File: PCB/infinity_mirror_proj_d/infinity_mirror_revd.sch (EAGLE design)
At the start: 28 parts, among them J1 5.5x2.1mm Barrel, Q1 800mA/40V, Q2 800mA/40V, U1 3.3LDO

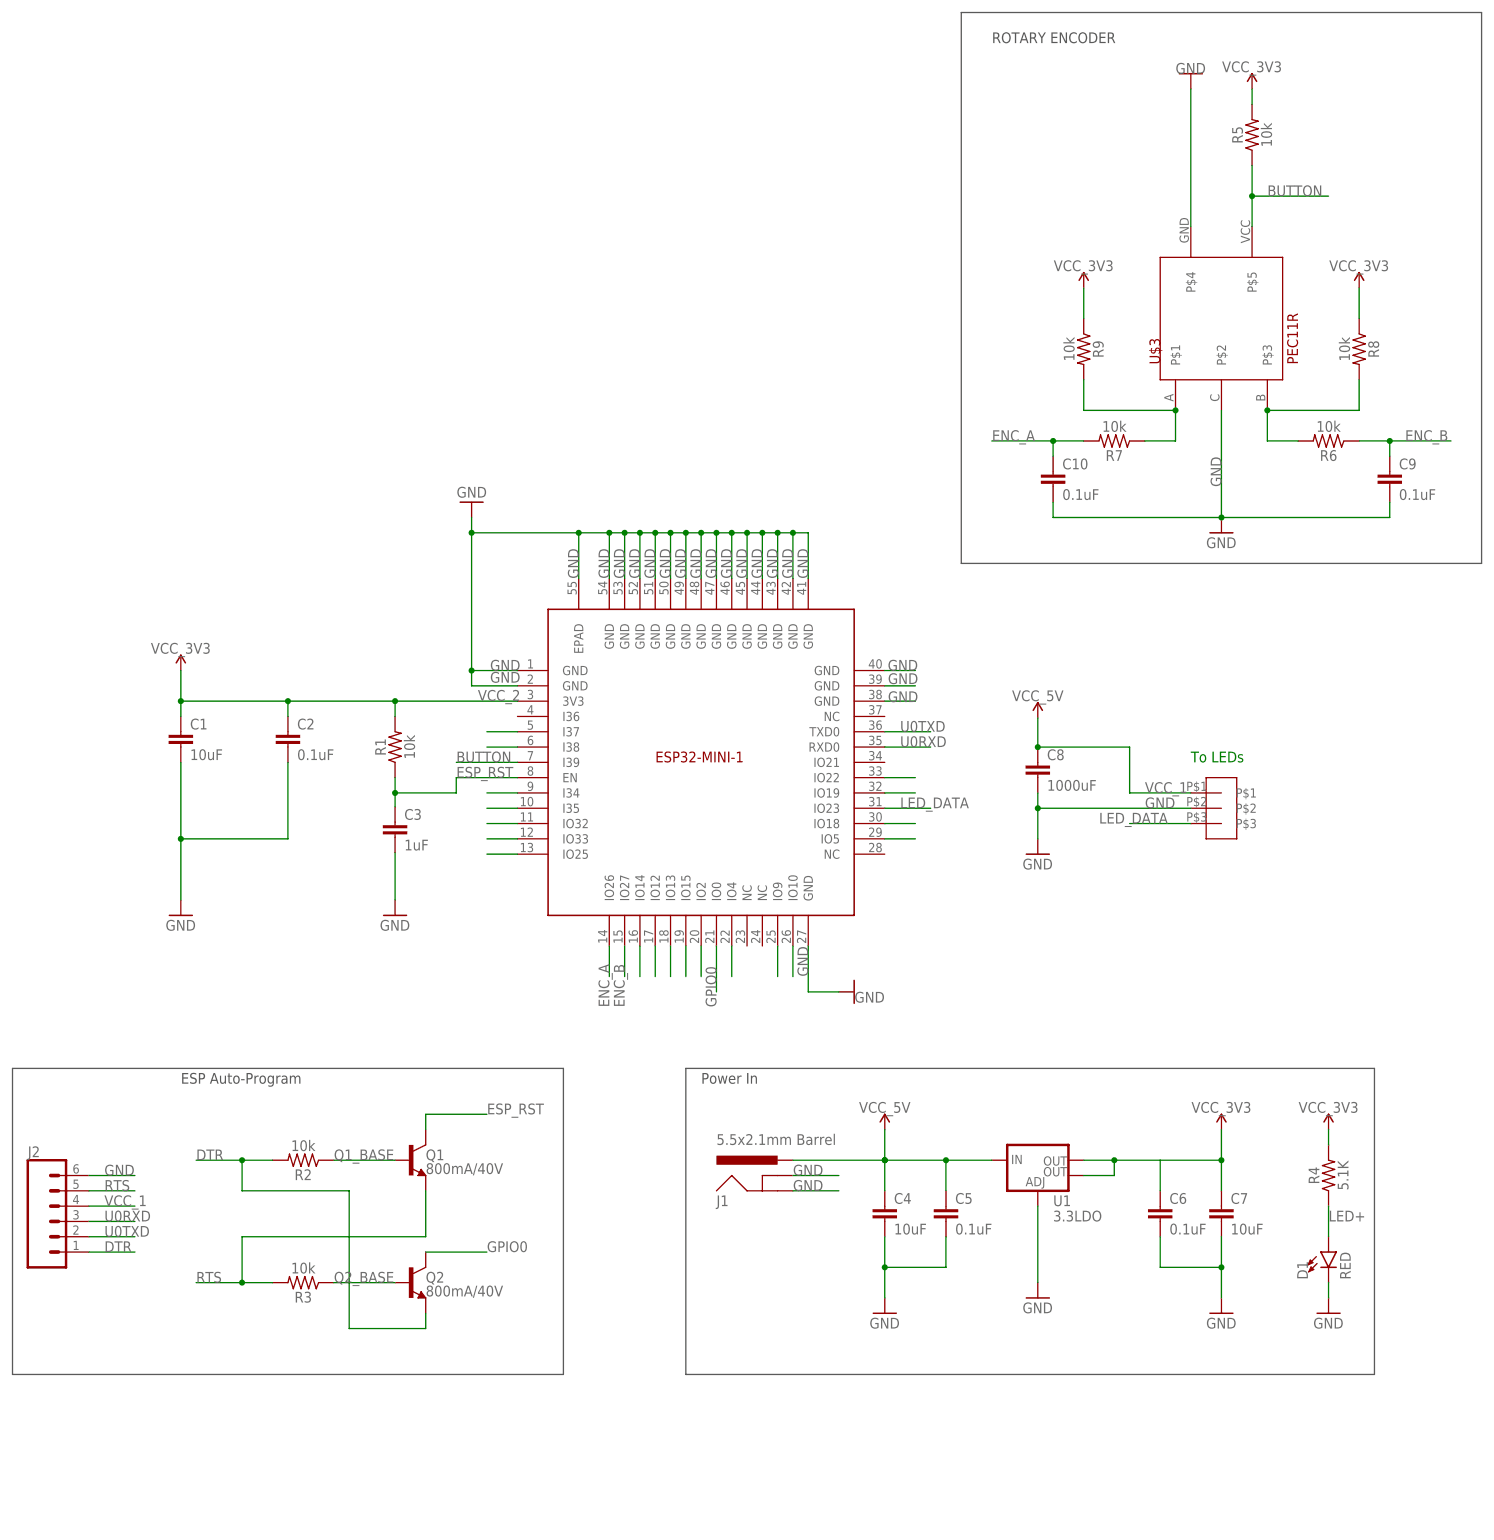
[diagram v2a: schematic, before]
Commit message: added logic level shifting for LEDs and buttons for programming
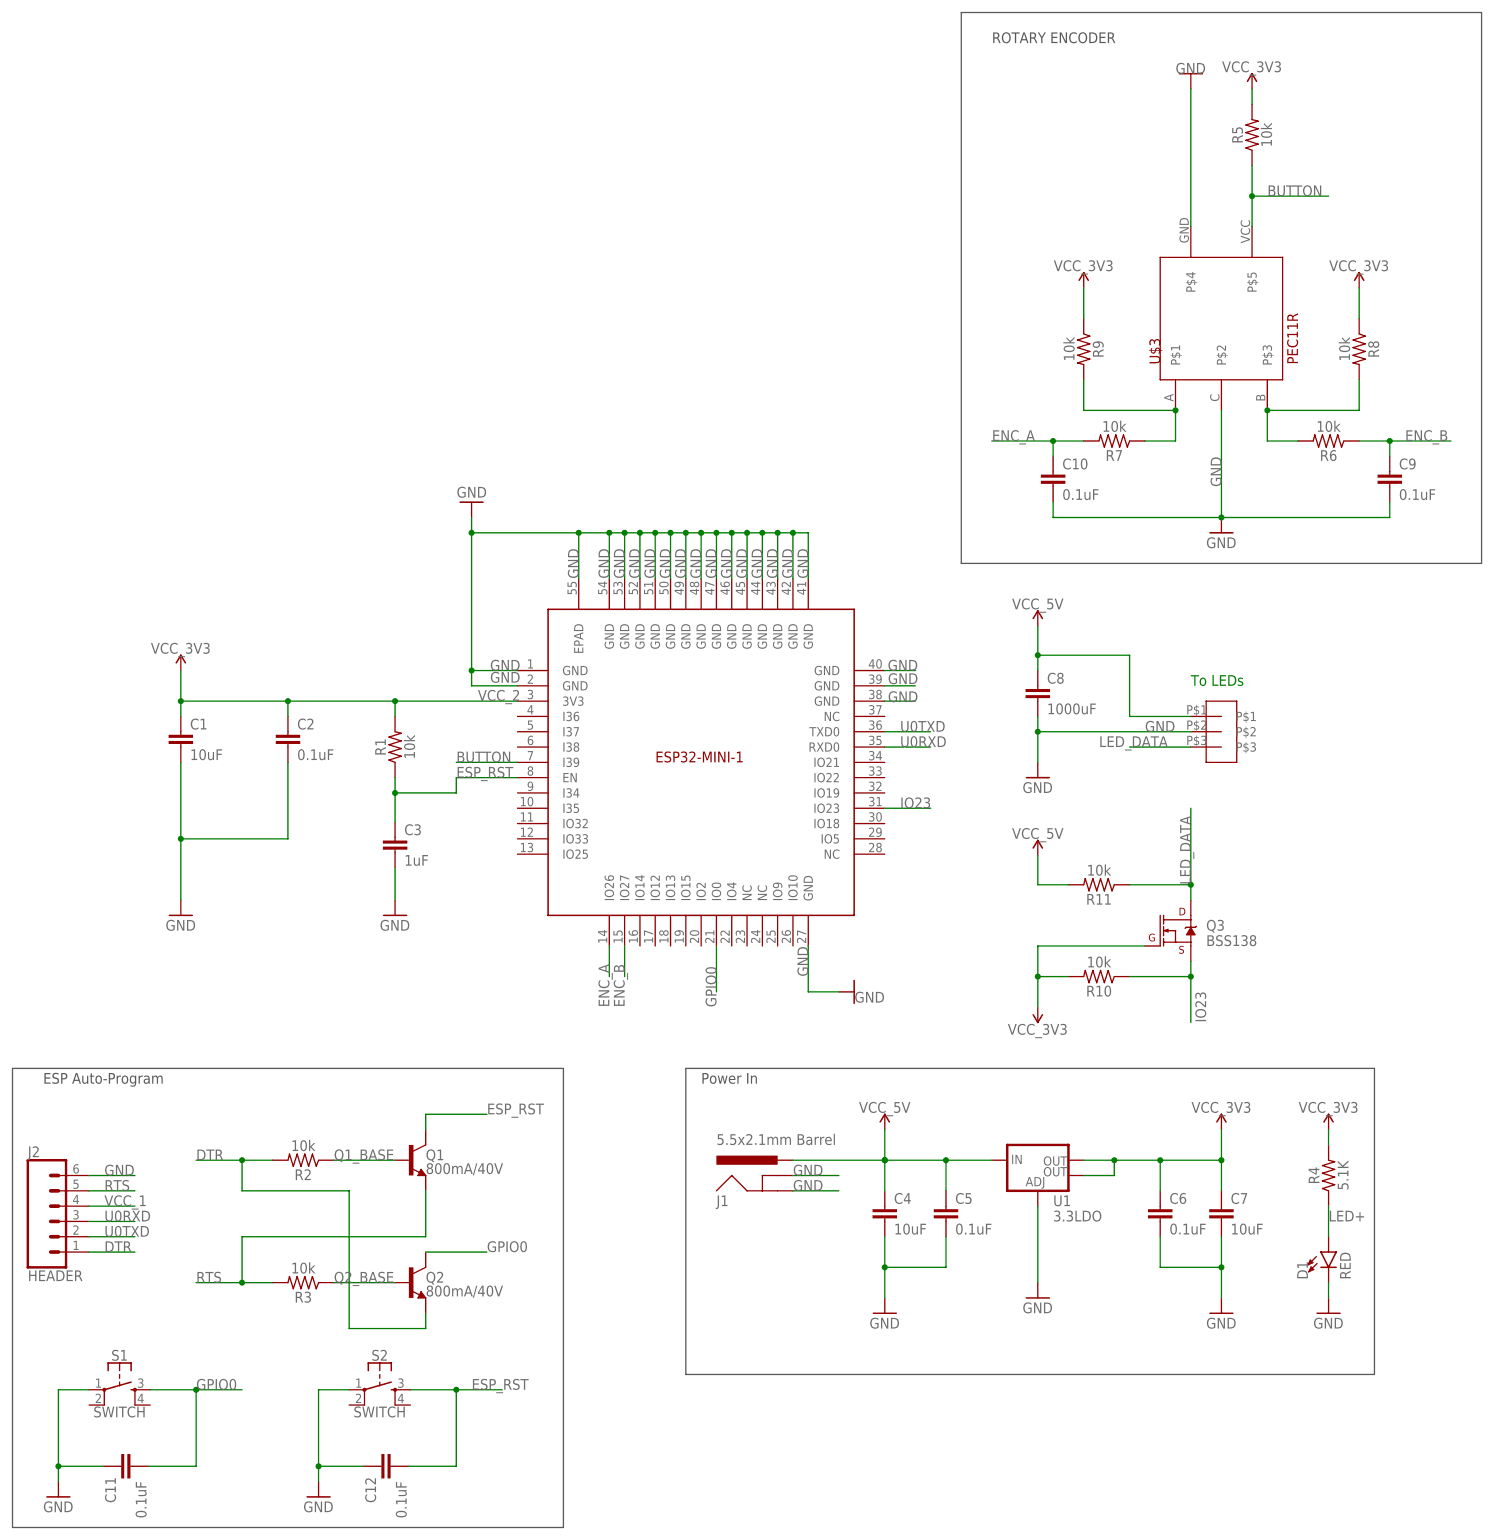
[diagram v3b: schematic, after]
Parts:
- added C11, C12: 0.1uF, _111_IH:CAPACITOR
- added Q3: BSS138, SparkFun-DiscreteSemi:MOSFET-NCH-BSS138
- added R10, R11: 10k, _111_IH:RESISTOR
- added S1, S2: SWITCH, SparkFun-Switches:MOMENTARY-SWITCH-SPST-2-SMD-5.2MM-TALL
- J2: value (none) -> HEADER
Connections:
- removed net N$1: U$1.I35
- removed net N$11: U$1.IO32
- removed net N$12: U$1.IO33
- removed net N$13: U$1.IO25
- removed net N$17: U$1.IO5
- removed net N$18: U$1.IO18
- removed net N$20: U$1.IO19
- removed net N$21: U$1.IO22
- removed net N$24: U$1.IO10
- removed net N$25: U$1.IO9
- removed net N$28: U$1.IO4
- removed net N$30: U$1.IO2
- removed net N$31: U$1.IO15
- removed net N$32: U$1.IO13
- removed net N$33: U$1.IO12
- removed net N$34: U$1.IO14
- removed net N$5: U$1.I37
- removed net N$6: U$1.I38
- removed net N$9: U$1.I34
- new net IO23: Q3.S, R10.1, U$1.IO23
- net ESP_RST: now also C12.2, S2.3
- net GND: now also C11.1, C12.1, S1.1, S2.1
- net GPIO0: now also C11.2, S1.3
- net LED_DATA: now also Q3.D, R11.1; no longer U$1.IO23
- net VCC_1: now also R11.2
- net VCC_2: now also Q3.G, R10.2
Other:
- moved on the sheet: C3, C8

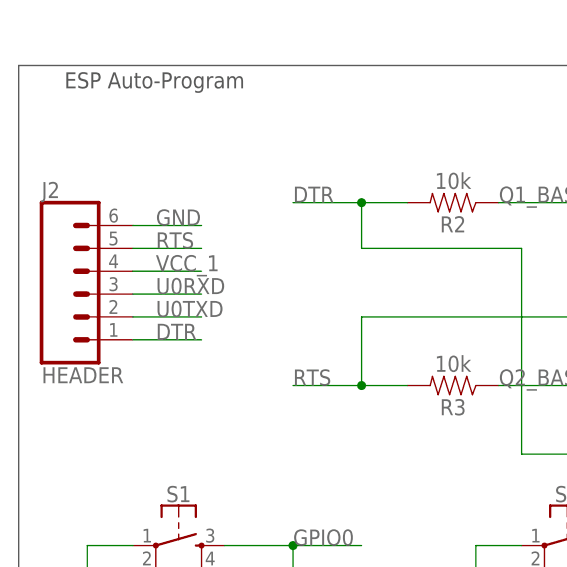
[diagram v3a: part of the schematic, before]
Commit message: fixed airwires and changed programming header from 6 pins to 4 pins
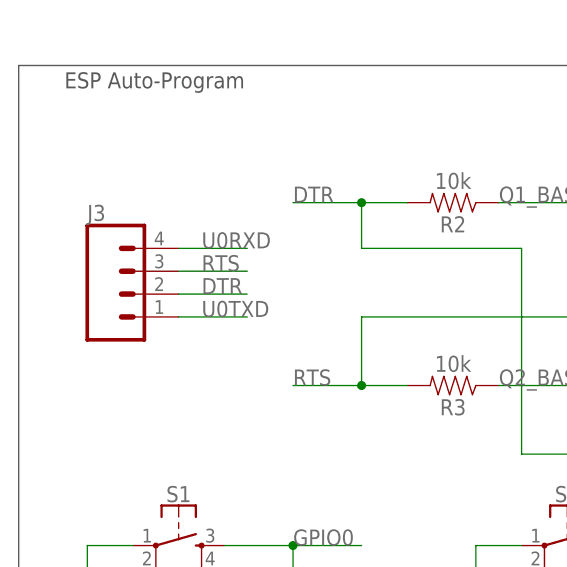
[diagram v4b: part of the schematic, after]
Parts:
- removed J2: HEADER, SparkFun-Connectors:CONN_06SILK_FEMALE_PTH
- added J3: (no value), SparkFun-Connectors:CONN_04
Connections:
- net DTR: now also J3.2; no longer J2.1
- net GND: no longer J2.6
- net RTS: now also J3.3; no longer J2.5
- net U0RXD: now also J3.4; no longer J2.3
- net U0TXD: now also J3.1; no longer J2.2
- net VCC_1: no longer J2.4
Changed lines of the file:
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@@
 <?xml version="1.0" encoding="utf-8"?>
 <!DOCTYPE eagle SYSTEM "eagle.dtd">
-<eagle version="9.6.2">
+<eagle version="9.3.0">
 <drawing>
 <settings>
@@
 <part name="R7" library="_111_IH" deviceset="RESISTOR" device="" value="10k"/>
 <part name="C10" library="_111_IH" deviceset="CAPACITOR" device="" value="0.1uF"/>
-<part name="J2" library="SparkFun-Connectors" deviceset="CONN_06" device="SILK_FEMALE_PTH" value="HEADER"/>
 <part name="R8" library="_111_IH" deviceset="RESISTOR" device="" value="10k"/>
 <part name="R9" library="_111_IH" deviceset="RESISTOR" device="" value="10k"/>
@@
 <part name="GND12" library="supply1" library_urn="urn:adsk.eagle:library:371" deviceset="GND" device=""/>
 <part name="GND13" library="supply1" library_urn="urn:adsk.eagle:library:371" deviceset="GND" device=""/>
+<part name="J3" library="SparkFun-Connectors" deviceset="CONN_04" device=""/>
 </parts>
 <sheets>
@@
 <attribute name="VALUE" x="59.944" y="43.561" size="1.778" layer="96" font="vector"/>
 </instance>
-<instance part="J2" gate="G$1" x="-106.68" y="-76.2" smashed="yes">
-<attribute name="VALUE" x="-111.76" y="-86.106" size="1.778" layer="96" font="vector"/>
-<attribute name="NAME" x="-111.76" y="-65.532" size="1.778" layer="95" font="vector"/>
-</instance>
 <instance part="R8" gate="G$1" x="109.22" y="68.58" smashed="yes" rot="R270">
 <attribute name="NAME" x="110.744" y="68.58" size="1.778" layer="95" font="vector" rot="R270" align="bottom-center"/>
@@
 <instance part="GND13" gate="1" x="-63.5" y="-121.92" smashed="yes">
 <attribute name="VALUE" x="-66.04" y="-124.46" size="1.778" layer="96"/>
+</instance>
+<instance part="J3" gate="G$1" x="-101.6" y="-76.2" smashed="yes">
+<attribute name="VALUE" x="-106.68" y="-83.566" size="1.778" layer="96" font="vector"/>
+<attribute name="NAME" x="-106.68" y="-68.072" size="1.778" layer="95" font="vector"/>
 </instance>
 </instances>
@@
 </segment>
 <segment>
-<pinref part="J2" gate="G$1" pin="2"/>
-<wire x1="-101.6" y1="-78.74" x2="-93.98" y2="-78.74" width="0.1524" layer="91"/>
-<label x="-99.06" y="-78.74" size="1.778" layer="95"/>
+<pinref part="J3" gate="G$1" pin="1"/>
+<wire x1="-96.52" y1="-78.74" x2="-88.9" y2="-78.74" width="0.1524" layer="91"/>
+<label x="-93.98" y="-78.74" size="1.778" layer="95"/>
 </segment>
 </net>
@@
 </segment>
 <segment>
-<pinref part="J2" gate="G$1" pin="6"/>
-<wire x1="-101.6" y1="-68.58" x2="-93.98" y2="-68.58" width="0.1524" layer="91"/>
-<label x="-99.06" y="-68.58" size="1.778" layer="95"/>
-</segment>
-<segment>
 <pinref part="GND12" gate="1" pin="GND"/>
 <wire x1="-106.68" y1="-119.38" x2="-106.68" y2="-116.84" width="0.1524" layer="91"/>
@@
 </segment>
 <segment>
-<pinref part="J2" gate="G$1" pin="3"/>
-<wire x1="-101.6" y1="-76.2" x2="-93.98" y2="-76.2" width="0.1524" layer="91"/>
-<label x="-99.06" y="-76.2" size="1.778" layer="95"/>
+<pinref part="J3" gate="G$1" pin="4"/>
+<wire x1="-96.52" y1="-71.12" x2="-88.9" y2="-71.12" width="0.1524" layer="91"/>
+<label x="-93.98" y="-71.12" size="1.778" layer="95"/>
 </segment>
 </net>
@@
 </segment>
 <segment>
-<pinref part="J2" gate="G$1" pin="1"/>
-<wire x1="-101.6" y1="-81.28" x2="-93.98" y2="-81.28" width="0.1524" layer="91"/>
-<label x="-99.06" y="-81.28" size="1.778" layer="95"/>
+<pinref part="J3" gate="G$1" pin="2"/>
+<wire x1="-96.52" y1="-76.2" x2="-88.9" y2="-76.2" width="0.1524" layer="91"/>
+<label x="-93.98" y="-76.2" size="1.778" layer="95"/>
 </segment>
 </net>
@@
 </segment>
 <segment>
-<pinref part="J2" gate="G$1" pin="5"/>
-<wire x1="-101.6" y1="-71.12" x2="-93.98" y2="-71.12" width="0.1524" layer="91"/>
-<label x="-99.06" y="-71.12" size="1.778" layer="95"/>
+<pinref part="J3" gate="G$1" pin="3"/>
+<wire x1="-96.52" y1="-73.66" x2="-88.9" y2="-73.66" width="0.1524" layer="91"/>
+<label x="-93.98" y="-73.66" size="1.778" layer="95"/>
 </segment>
 </net>
@@
 <wire x1="55.88" y1="-20.32" x2="55.88" y2="-15.494" width="0.1524" layer="91"/>
 </segment>
-<segment>
-<pinref part="J2" gate="G$1" pin="4"/>
-<wire x1="-101.6" y1="-73.66" x2="-93.98" y2="-73.66" width="0.1524" layer="91"/>
-<label x="-99.06" y="-73.66" size="1.778" layer="95"/>
-</segment>
-</net>
+</net>

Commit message: more airwires. cleaned up silk. changed LED cap to leaded electrolytic
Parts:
- removed C8: 1000uF, _111_IH:CAPACITOR
- added J2: (no value), SparkFun-Connectors:CONN_02
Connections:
- new net N$1: J2.2
- net GND: no longer C8.2
- net VCC_1: now also J2.1; no longer C8.1
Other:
- note added: "Decoupling Cap"
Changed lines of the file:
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@@
 <part name="SUPPLY1" library="SparkFun-PowerSymbols" deviceset="VCC_2" device="" value="VCC_3V3"/>
 <part name="GND8" library="supply1" library_urn="urn:adsk.eagle:library:371" deviceset="GND" device=""/>
-<part name="C8" library="_111_IH" deviceset="CAPACITOR" device="" value="1000uF"/>
 <part name="U$2" library="infinity_mirror_revd" deviceset="3-PIN-JST" device=""/>
 <part name="SUPPLY5" library="SparkFun-PowerSymbols" deviceset="VCC_1" device="" value="VCC_5V"/>
@@
 <part name="GND13" library="supply1" library_urn="urn:adsk.eagle:library:371" deviceset="GND" device=""/>
 <part name="J3" library="SparkFun-Connectors" deviceset="CONN_04" device=""/>
+<part name="J2" library="SparkFun-Connectors" deviceset="CONN_02" device=""/>
 </parts>
 <sheets>
@@
 <wire x1="129.54" y1="124.46" x2="129.54" y2="33.02" width="0.1524" layer="97"/>
 <wire x1="129.54" y1="33.02" x2="43.18" y2="33.02" width="0.1524" layer="97"/>
+<text x="76.2" y="20.32" size="1.778" layer="91" rot="R180">Decoupling Cap</text>
 </plain>
 <instances>
@@
 <attribute name="VALUE" x="101.6" y="-93.98" size="1.778" layer="96"/>
 </instance>
-<instance part="C8" gate="G$1" x="55.88" y="10.146" smashed="yes">
-<attribute name="NAME" x="57.404" y="13.067" size="1.778" layer="95" font="vector"/>
-<attribute name="VALUE" x="57.404" y="7.987" size="1.778" layer="96" font="vector"/>
-</instance>
 <instance part="U$2" gate="G$1" x="86.36" y="5.08" smashed="yes"/>
 <instance part="SUPPLY5" gate="G$2" x="55.88" y="22.606" smashed="yes">
@@
 <attribute name="VALUE" x="-106.68" y="-83.566" size="1.778" layer="96" font="vector"/>
 <attribute name="NAME" x="-106.68" y="-68.072" size="1.778" layer="95" font="vector"/>
+</instance>
+<instance part="J2" gate="G$1" x="63.5" y="12.7" smashed="yes" rot="R180">
+<attribute name="VALUE" x="66.04" y="17.526" size="1.778" layer="96" font="vector" rot="R180"/>
+<attribute name="NAME" x="66.04" y="7.112" size="1.778" layer="95" font="vector" rot="R180"/>
 </instance>
 </instances>
@@
 <pinref part="U$2" gate="G$1" pin="P$2"/>
 <label x="73.66" y="5.08" size="1.778" layer="95"/>
-<pinref part="C8" gate="G$1" pin="2"/>
 <wire x1="55.88" y1="7.606" x2="55.88" y2="5.08" width="0.1524" layer="91"/>
 <wire x1="55.88" y1="5.08" x2="81.28" y2="5.08" width="0.1524" layer="91"/>
@@
 <wire x1="81.28" y1="7.62" x2="71.12" y2="7.62" width="0.1524" layer="91"/>
 <wire x1="71.12" y1="17.78" x2="71.12" y2="7.62" width="0.1524" layer="91"/>
-<pinref part="C8" gate="G$1" pin="1"/>
-<wire x1="55.88" y1="15.226" x2="55.88" y2="17.78" width="0.1524" layer="91"/>
+<wire x1="55.88" y1="15.226" x2="55.88" y2="15.24" width="0.1524" layer="91"/>
 <junction x="55.88" y="17.78"/>
+<pinref part="J2" gate="G$1" pin="1"/>
+<wire x1="55.88" y1="15.24" x2="55.88" y2="17.78" width="0.1524" layer="91"/>
+<wire x1="55.88" y1="12.7" x2="55.88" y2="15.226" width="0.1524" layer="91"/>
 </segment>
 <segment>
@@
 </segment>
 </net>
+<net name="N$1" class="0">
+<segment>
+<pinref part="J2" gate="G$1" pin="2"/>
+<wire x1="55.88" y1="10.16" x2="55.88" y2="7.62" width="0.1524" layer="91"/>
+</segment>
+</net>

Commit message: not sure
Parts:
- J1: value 5.5x2.1mm Barrel -> POWER_JACKPTH_BREAD; device SparkFun-Connectors:POWER_JACKSMD -> SparkFun-Connectors:POWER_JACKPTH_BREAD
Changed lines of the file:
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@@
 <part name="R3" library="_111_IH" deviceset="RESISTOR" device="" value="10k"/>
 <part name="Q2" library="SparkFun-DiscreteSemi" deviceset="TRANS_NPN" device="-MMBT2222AL" value="800mA/40V"/>
-<part name="J1" library="SparkFun-Connectors" deviceset="POWER_JACK" device="SMD" value="5.5x2.1mm Barrel"/>
+<part name="J1" library="SparkFun-Connectors" library_urn="urn:adsk.eagle:library:513" deviceset="POWER_JACK" device="PTH_BREAD" package3d_urn="urn:adsk.eagle:package:38228/1" value="POWER_JACKPTH_BREAD"/>
 <part name="U1" library="SparkFun-IC-Power" library_urn="urn:adsk.eagle:library:526" deviceset="V_REG_LM1117" device="SOT223" package3d_urn="urn:adsk.eagle:package:39069/1" value="3.3LDO"/>
 <part name="GND5" library="supply1" library_urn="urn:adsk.eagle:library:371" deviceset="GND" device=""/>
@@
 </instance>
 <instance part="J1" gate="G$1" x="12.7" y="-73.66" smashed="yes">
-<attribute name="VALUE" x="2.54" y="-63.5" size="1.778" layer="96" font="vector"/>
 <attribute name="NAME" x="2.54" y="-73.66" size="1.778" layer="95" font="vector"/>
 </instance>
